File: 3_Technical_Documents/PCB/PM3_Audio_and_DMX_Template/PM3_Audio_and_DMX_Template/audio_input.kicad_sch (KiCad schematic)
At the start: 37 parts, among them U10 OPA2134, U11 OPA2134, U5 OPA2134

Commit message: new push
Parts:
- removed C39, C48, C75: 10n COG/X7R, Capacitor_SMD:C_0603_1608Metric, symbol Device:C
- removed C42: 1u ELEC, Capacitor_SMD:CP_Elec_4x5.8, symbol Device:C_Polarized
- removed C73, C74: 10u, Capacitor_SMD:CP_Elec_4x5.8, symbol Device:C_Polarized
- removed C76, C77: 470p COG/X7R, Capacitor_SMD:C_0603_1608Metric, symbol Device:C
- removed C78: 2n7 COG/X7R, Capacitor_SMD:C_0603_1608Metric, symbol Device:C
- removed R47, R48, R8, R9: 10k, Resistor_SMD:R_0603_1608Metric, symbol Device:R
- removed R49, R50: 634R, Resistor_SMD:R_0603_1608Metric, symbol Device:R
- removed R51, R52: 91R, Resistor_SMD:R_0603_1608Metric, symbol Device:R
- removed unit 1 of U5
- removed unit 2 of U5
- added C32: 2n7 COG/X7R, Capacitor_SMD:C_0603_1608Metric, symbol Device:C
- renumbered C81 to C45, C79 to C46, C12 to C47, C82 to C50, C80 to C51, C11 to C52, C43 to C53, C40 to C54, C46 to C59, C45 to C60, C44 to C63, R19 to R33, R18 to R34, R22 to R37, R20 to R38, R23 to R41, R21 to R42, U10 to U11, U11 to U12, U5 to U12, U11 to U13
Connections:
- net AINB: now also R38.2, R42.2, C32.2
- net GND: no longer U11.5 (+), U11.6 (-)
- net VCOM: now also C63.2, U11.5 (+), C32.1
- net at U11.7: now also U11.6 (-)
- removed net VQ2: C63.2, R38.2, R42.2
- no-connect marks 1 -> 0
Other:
- moved on the sheet: C45, C46, C47, C50, C51, C52, C53, C54, C59, C60, C63, R33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

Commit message: rework esp32, codec and layout
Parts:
- removed C47: 10n COG/X7R, Capacitor_SMD:C_0603_1608Metric, symbol Device:C
- removed C52: 1u ELEC, Capacitor_SMD:CP_Elec_4x5.8, symbol Device:C_Polarized
- removed U13: OPA2134, Package_SO:SOIC-8_3.9x4.9mm_P1.27mm, symbol Amplifier_Operational:OPA2134
- renumbered C53 to C42, C54 to C43, C59 to C44, C60 to C45, C63 to C46, C32 to C47, C45 to C48, C46 to C49, R33 to R37, R34 to R38, R37 to R39, R38 to R40, U12 to U11, U11 to U12

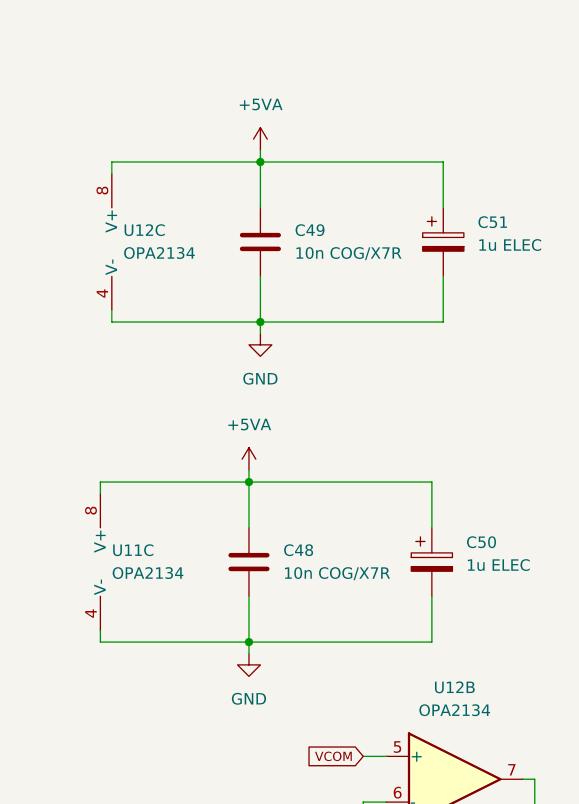
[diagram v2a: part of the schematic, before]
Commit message: updated capacitors
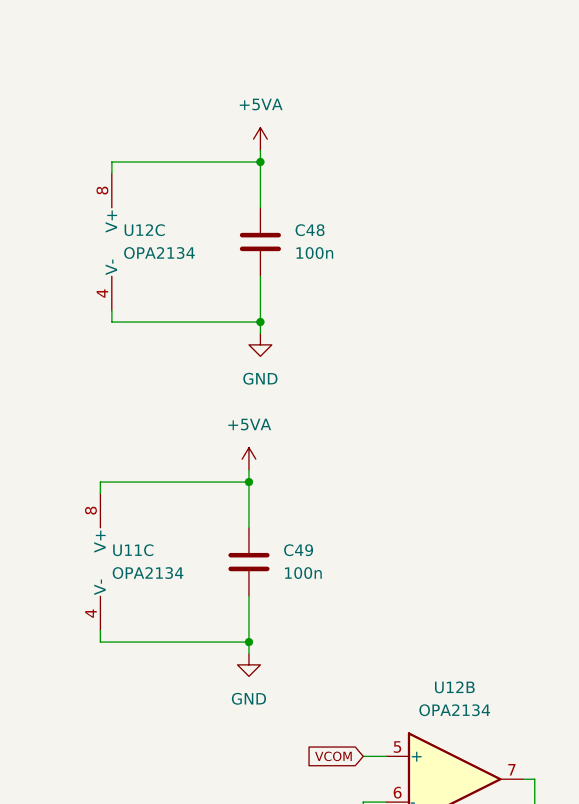
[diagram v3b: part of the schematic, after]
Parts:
- removed C50, C51: 1u ELEC, Capacitor_SMD:CP_Elec_4x5.8, symbol Device:C_Polarized
- C48, C49: value 10n COG/X7R -> 100n; MPN GPC0603103 -> GPC0603104-X7R

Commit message: esp-stm connection (+ conflict recolution)
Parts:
- U11, U12: footprint (none) -> Package_SO:SOIC-8_3.9x4.9mm_P1.27mm
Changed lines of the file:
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@@
 			)
 		)
-		(property "Footprint" ""
+		(property "Footprint" "Package_SO:SOIC-8_3.9x4.9mm_P1.27mm"
 			(at 269.24 139.7 0)
 			(effects
@@
 					(reference "U12")
 					(unit 2)
-				)
-			)
-		)
-	)
-	(symbol
-		(lib_id "Device:C")
-		(at 246.38 115.57 0)
-		(unit 1)
-		(exclude_from_sim no)
-		(in_bom yes)
-		(on_board yes)
-		(dnp no)
-		(fields_autoplaced yes)
-		(property "Reference" "C49"
-			(at 250.19 114.2999 0)
-			(effects
-				(font
-					(size 1.27 1.27)
-				)
-				(justify left)
-			)
-		)
-		(property "Value" "100n"
-			(at 250.19 116.8399 0)
-			(effects
-				(font
-					(size 1.27 1.27)
-				)
-				(justify left)
-			)
-		)
-		(property "Footprint" "Capacitor_SMD:C_0603_1608Metric"
-			(at 247.3452 119.38 0)
-			(effects
-				(font
-					(size 1.27 1.27)
-				)
-				(hide yes)
-			)
-		)
-		(property "Datasheet" "~"
-			(at 246.38 115.57 0)
-			(effects
-				(font
-					(size 1.27 1.27)
-				)
-				(hide yes)
-			)
-		)
-		(property "Description" "Unpolarized capacitor"
-			(at 246.38 115.57 0)
-			(effects
-				(font
-					(size 1.27 1.27)
-				)
-				(hide yes)
-			)
-		)
-		(property "MPN" "GPC0603104-X7R"
-			(at 246.38 115.57 0)
-			(effects
-				(font
-					(size 1.27 1.27)
-				)
-				(hide yes)
-			)
-		)
-		(property "Manufacturer" ""
-			(at 246.38 115.57 0)
-			(effects
-				(font
-					(size 1.27 1.27)
-				)
-				(hide yes)
-			)
-		)
-		(pin "1"
-		)
-		(pin "2"
-		)
-		(instances
-			(project "PM3_Audio_and_DMX"
-				(path "/1f276d59-ad9b-4e70-a842-f3b7e562eb9b/2329d9ea-d5d7-4913-84c5-e85a54af032e/5f71fd42-8f86-4900-bb58-dbcd17a8cc2c/8717c379-1954-44ba-9e1e-6e736552020c"
-					(reference "C49")
-					(unit 1)
 				)
 			)
@@
 	)
 	(symbol
+		(lib_id "Device:C")
+		(at 247.65 80.01 0)
+		(unit 1)
+		(exclude_from_sim no)
+		(in_bom yes)
+		(on_board yes)
+		(dnp no)
+		(fields_autoplaced yes)
+		(property "Reference" "C49"
+			(at 251.46 78.7399 0)
+			(effects
+				(font
+					(size 1.27 1.27)
+				)
+				(justify left)
+			)
+		)
+		(property "Value" "100n"
+			(at 251.46 81.2799 0)
+			(effects
+				(font
+					(size 1.27 1.27)
+				)
+				(justify left)
+			)
+		)
+		(property "Footprint" "Capacitor_SMD:C_0603_1608Metric"
+			(at 248.6152 83.82 0)
+			(effects
+				(font
+					(size 1.27 1.27)
+				)
+				(hide yes)
+			)
+		)
+		(property "Datasheet" "~"
+			(at 247.65 80.01 0)
+			(effects
+				(font
+					(size 1.27 1.27)
+				)
+				(hide yes)
+			)
+		)
+		(property "Description" "Unpolarized capacitor"
+			(at 247.65 80.01 0)
+			(effects
+				(font
+					(size 1.27 1.27)
+				)
+				(hide yes)
+			)
+		)
+		(property "MPN" "GPC0603104-X7R"
+			(at 247.65 80.01 0)
+			(effects
+				(font
+					(size 1.27 1.27)
+				)
+				(hide yes)
+			)
+		)
+		(property "Manufacturer" ""
+			(at 247.65 80.01 0)
+			(effects
+				(font
+					(size 1.27 1.27)
+				)
+				(hide yes)
+			)
+		)
+		(pin "2"
+		)
+		(pin "1"
+		)
+		(instances
+			(project "PM3_Audio_and_DMX"
+				(path "/1f276d59-ad9b-4e70-a842-f3b7e562eb9b/2329d9ea-d5d7-4913-84c5-e85a54af032e/5f71fd42-8f86-4900-bb58-dbcd17a8cc2c/8717c379-1954-44ba-9e1e-6e736552020c"
+					(reference "C49")
+					(unit 1)
+				)
+			)
+		)
+	)
+	(symbol
+		(lib_id "Device:C")
+		(at 246.38 115.57 0)
+		(unit 1)
+		(exclude_from_sim no)
+		(in_bom yes)
+		(on_board yes)
+		(dnp no)
+		(fields_autoplaced yes)
+		(property "Reference" "C48"
+			(at 250.19 114.2999 0)
+			(effects
+				(font
+					(size 1.27 1.27)
+				)
+				(justify left)
+			)
+		)
+		(property "Value" "100n"
+			(at 250.19 116.8399 0)
+			(effects
+				(font
+					(size 1.27 1.27)
+				)
+				(justify left)
+			)
+		)
+		(property "Footprint" "Capacitor_SMD:C_0603_1608Metric"
+			(at 247.3452 119.38 0)
+			(effects
+				(font
+					(size 1.27 1.27)
+				)
+				(hide yes)
+			)
+		)
+		(property "Datasheet" "~"
+			(at 246.38 115.57 0)
+			(effects
+				(font
+					(size 1.27 1.27)
+				)
+				(hide yes)
+			)
+		)
+		(property "Description" "Unpolarized capacitor"
+			(at 246.38 115.57 0)
+			(effects
+				(font
+					(size 1.27 1.27)
+				)
+				(hide yes)
+			)
+		)
+		(property "MPN" "GPC0603104-X7R"
+			(at 246.38 115.57 0)
+			(effects
+				(font
+					(size 1.27 1.27)
+				)
+				(hide yes)
+			)
+		)
+		(property "Manufacturer" ""
+			(at 246.38 115.57 0)
+			(effects
+				(font
+					(size 1.27 1.27)
+				)
+				(hide yes)
+			)
+		)
+		(pin "2"
+		)
+		(pin "1"
+		)
+		(instances
+			(project "PM3_Audio_and_DMX"
+				(path "/1f276d59-ad9b-4e70-a842-f3b7e562eb9b/2329d9ea-d5d7-4913-84c5-e85a54af032e/5f71fd42-8f86-4900-bb58-dbcd17a8cc2c/8717c379-1954-44ba-9e1e-6e736552020c"
+					(reference "C48")
+					(unit 1)
+				)
+			)
+		)
+	)
+	(symbol
 		(lib_id "Device:R")
 		(at 88.9 71.12 180)
@@
 			)
 		)
-		(property "Footprint" ""
+		(property "Footprint" "Package_SO:SOIC-8_3.9x4.9mm_P1.27mm"
 			(at 134.62 121.92 0)
 			(effects
@@
 			)
 		)
-		(property "Footprint" ""
+		(property "Footprint" "Package_SO:SOIC-8_3.9x4.9mm_P1.27mm"
 			(at 232.41 115.57 0)
 			(effects
@@
 					(unit 1)
 				)
-			)
-		)
-	)
-	(symbol
-		(lib_id "Device:C")
-		(at 247.65 80.01 0)
-		(unit 1)
-		(exclude_from_sim no)
-		(in_bom yes)
-		(on_board yes)
-		(dnp no)
-		(fields_autoplaced yes)
-		(property "Reference" "C48"
-			(at 251.46 78.7399 0)
-			(effects
-				(font
-					(size 1.27 1.27)
-				)
-				(justify left)
-			)
-		)
-		(property "Value" "100n"
-			(at 251.46 81.2799 0)
-			(effects
-				(font
-					(size 1.27 1.27)
-				)
-				(justify left)
-			)
-		)
-		(property "Footprint" "Capacitor_SMD:C_0603_1608Metric"
-			(at 248.6152 83.82 0)
-			(effects
-				(font
-					(size 1.27 1.27)
-				)
-				(hide yes)
-			)
-		)
-		(property "Datasheet" "~"
-			(at 247.65 80.01 0)
-			(effects
-				(font
-					(size 1.27 1.27)
-				)
-				(hide yes)
-			)
-		)
-		(property "Description" "Unpolarized capacitor"
-			(at 247.65 80.01 0)
-			(effects
-				(font
-					(size 1.27 1.27)
-				)
-				(hide yes)
-			)
-		)
-		(property "MPN" "GPC0603104-X7R"
-			(at 247.65 80.01 0)
-			(effects
-				(font
-					(size 1.27 1.27)
-				)
-				(hide yes)
-			)
-		)
-		(property "Manufacturer" ""
-			(at 247.65 80.01 0)
-			(effects
-				(font
-					(size 1.27 1.27)
-				)
-				(hide yes)
-			)
-		)
-		(pin "1"
-		)
-		(pin "2"
-		)
-		(instances
-			(project "PM3_Audio_and_DMX"
-				(path "/1f276d59-ad9b-4e70-a842-f3b7e562eb9b/2329d9ea-d5d7-4913-84c5-e85a54af032e/5f71fd42-8f86-4900-bb58-dbcd17a8cc2c/8717c379-1954-44ba-9e1e-6e736552020c"
-					(reference "C48")
-					(unit 1)
-				)

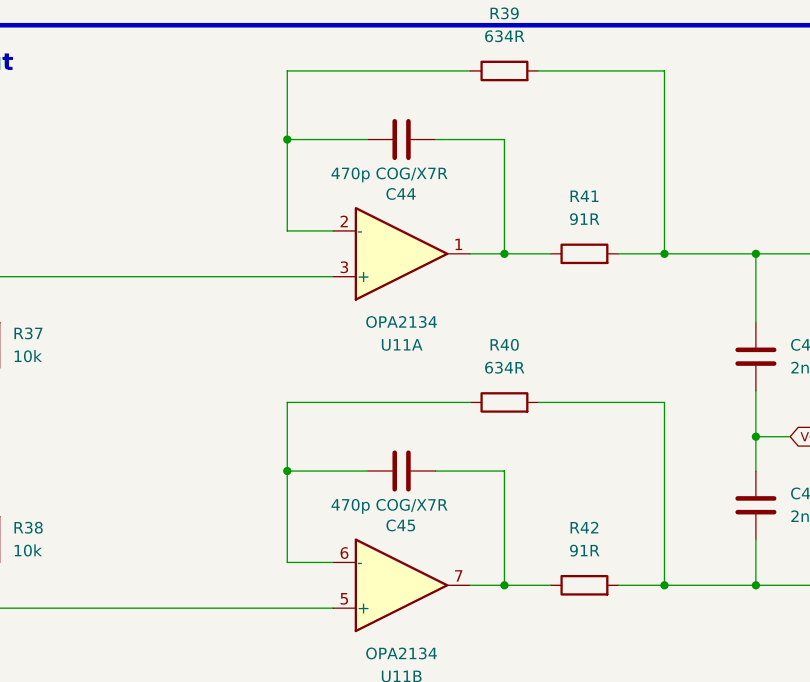
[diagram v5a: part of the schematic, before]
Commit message: schematics, layout and bom updated (to match corrections)
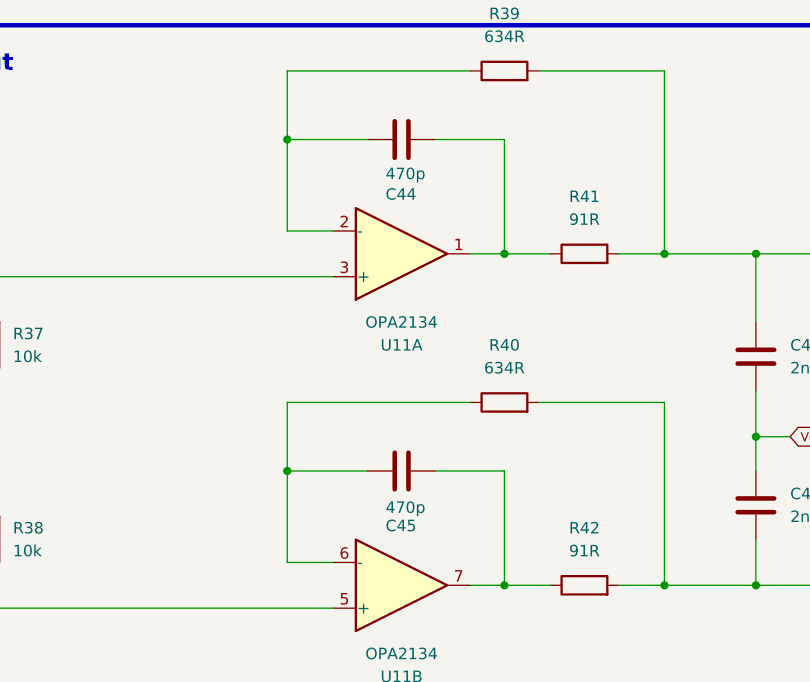
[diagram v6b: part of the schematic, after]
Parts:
- C44, C45: value 470p COG/X7R -> 470p
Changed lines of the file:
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@@
 			)
 		)
-		(property "Value" "470p COG/X7R"
-			(at 126.746 88.9 90)
+		(property "Value" "470p"
+			(at 132.842 89.154 90)
 			(effects
 				(font
@@
 			)
 		)
-		(property "Value" "470p COG/X7R"
-			(at 126.746 52.07 90)
-			(effects
-				(font
+		(property "Value" "470p"
+			(at 132.842 52.07 90)
+			(effects
+				(font
